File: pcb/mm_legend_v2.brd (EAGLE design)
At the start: 100 x 80 mm, 76 parts, among them IC1 ULN2003AD, IC2 TB6612FNG

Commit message: pcb: minor changes in pcb and schematic.
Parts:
- C17: value 100u -> 100n
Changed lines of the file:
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@@
 <element name="C15" library="resistor" package="B/3528-21W" value="47u" x="11.43" y="42.244" rot="R270"/>
 <element name="C16" library="resistor" package="A/3216-18R" value="10u" x="75.692" y="49.022" rot="R270"/>
-<element name="C17" library="resistor" package="C0805K" value="100u" x="30.988" y="40.64"/>
+<element name="C17" library="resistor" package="C0805K" value="100n" x="30.988" y="40.64"/>
 <element name="C18" library="resistor" package="C/6032-28R" value="100u" x="24.638" y="34.29"/>
 <element name="C19" library="resistor" package="C0805K" value="100n" x="30.988" y="45.466"/>

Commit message: pcb: redesigned pcb.
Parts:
- moved R6 39.0 mm to (19.3, 53.8), turned to 270 degrees
- moved R8 35.7 mm to (43.9, 57.7), turned to 90 degrees
- moved R7 35.0 mm to (16.5, 53.8), turned to 90 degrees
- moved R9 32.3 mm to (40.7, 57.7)
- moved R5 16.4 mm to (18.9, 46.0), turned to 270 degrees
- moved BAT_LED 15.6 mm to (18.9, 41.4), turned to 0 degrees
- moved R21 12.5 mm to (77.5, 65.5), turned to 270 degrees
- moved C18 11.8 mm to (26.2, 46.0)
- moved R20 11.5 mm to (85.6, 21.3), turned to 180 degrees
- moved L1 11.4 mm to (7.54, 35.6), turned to 0 degrees
- moved R10 9.80 mm to (76.5, 54.1)
- moved C20 9.74 mm to (28.2, 43.2), turned to 180 degrees
- moved C3 9.58 mm to (73.7, 38.4)
- moved C17 9.57 mm to (39.9, 37.1), turned to 90 degrees
- moved C19 9.45 mm to (38.6, 39.9)
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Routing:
- net GND: track 70.8 -> 237.8 mm, vias 14 -> 6
- net VBAT: track 108.6 -> 57.8 mm, vias 4 -> 2
- net MOTOR2_PWM: track 50.3 -> 83.1 mm, vias 2 -> 6
- net MOTOR1_PWM: track 50.7 -> 72.9 mm, vias 2 -> 6
- net N$15: track 2.39 -> 20.7 mm, vias 0 -> 2
- net PHOTO_FRONT_R: track 45.1 -> 63.4 mm
- net UI_LED: track 44.2 -> 26.9 mm, vias 0 -> 2
- net N$16: track 5.54 -> 22.1 mm, vias 0 -> 2
- net N$22: track 19.8 -> 6.08 mm
- net MOTOR2_CH1: track 43.8 -> 31.5 mm
- net N$8: track 43.6 -> 31.3 mm
- net N$10: track 17.9 -> 5.75 mm
- net MOTOR1_CH2: track 40.4 -> 29.3 mm
- net N$14: track 47.2 -> 36.7 mm
- net N$20: track 7.23 -> 17.4 mm
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
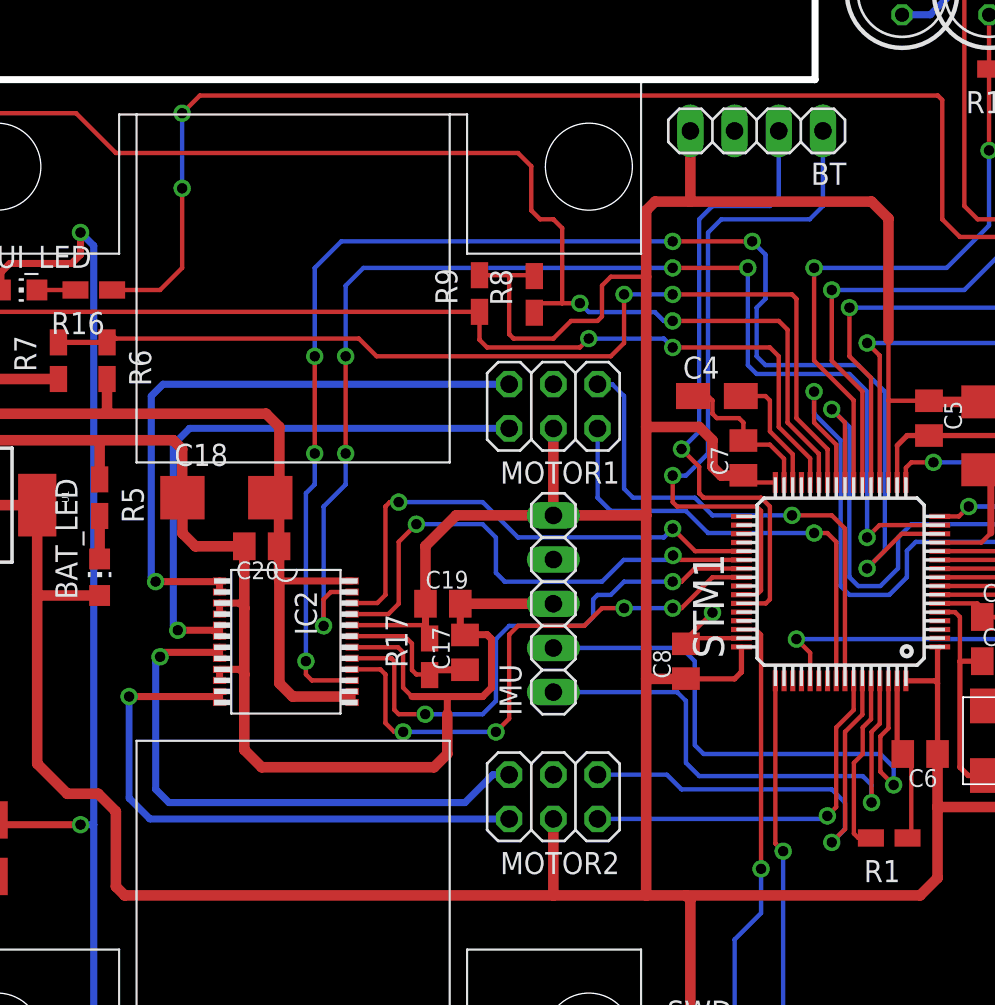
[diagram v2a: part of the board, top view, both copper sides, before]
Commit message: pcb: update pcb and schematic.
Changes:
- Moved BT connector away from motor holder.
- Changed pinout of motor connectors - fix issue #1.
- Added thicker lines for motor + and - signals.
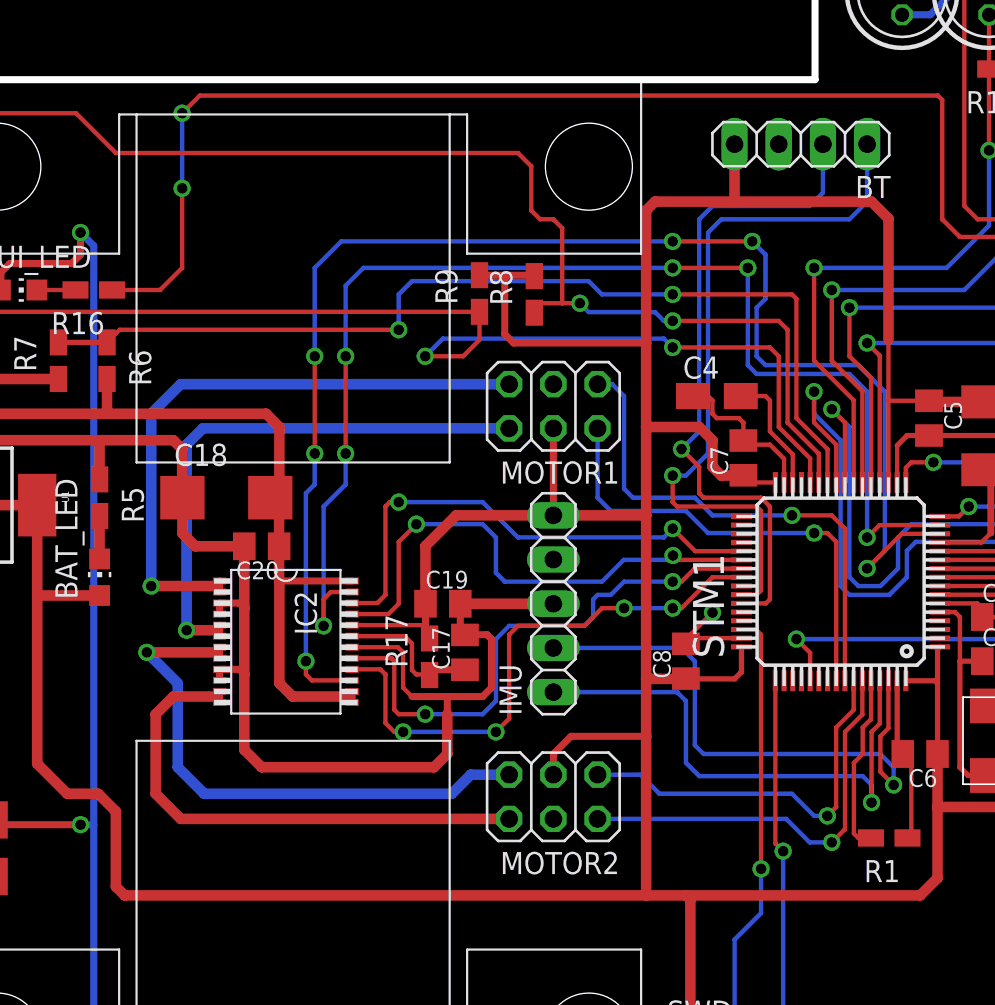
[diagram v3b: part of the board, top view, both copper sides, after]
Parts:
- moved BT 2.65 mm to (59.2, 66.3)
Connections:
- net 3V3: now also MOTOR2.3; no longer MOTOR2.4
- net ENC2_A: now also MOTOR2.1; no longer MOTOR2.2
- net ENC2_B: now also MOTOR2.2; no longer MOTOR2.1
- net GND: now also MOTOR2.4; no longer MOTOR2.3
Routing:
- net SW2: track 68.8 -> 75.5 mm
- net N$28: track 34.1 -> 30.3 mm, vias 1 -> 0
- net ENC2_B: track 27.5 -> 24.0 mm
- net USART_TX: track 39.4 -> 41.1 mm
- net USART_RX: track 36.9 -> 38.6 mm
- net N$24: track 33.6 -> 32.3 mm
- net VBAT: track 57.8 -> 56.8 mm
- net ENC2_A: track 21.7 -> 22.6 mm
- net N$30: track 33.3 -> 32.4 mm

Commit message: pcb: updated vbat resistors to real values.
Until now resistor values were 20k and 100k. 20k resistor doesn't exist in the series.
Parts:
- R3: value 100k -> 68k
- R4: value 20k -> 13k
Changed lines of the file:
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@@
 <element name="R22" library="resistor" package="R0805W" value="1k" x="91.186" y="28.956" rot="R90"/>
 <element name="R23" library="resistor" package="R0805W" value="1k" x="94.996" y="54.356" rot="R270"/>
-<element name="R3" library="resistor" package="R0805W" value="100k" x="9.144" y="27.512"/>
-<element name="R4" library="resistor" package="R0805W" value="20k" x="8.128" y="24.304" rot="R90"/>
+<element name="R3" library="resistor" package="R0805W" value="68k" x="9.144" y="27.512"/>
+<element name="R4" library="resistor" package="R0805W" value="13k" x="8.128" y="24.304" rot="R90"/>
 <element name="R5" library="resistor" package="R0805W" value="1k" x="18.876" y="45.974" rot="R270"/>
 <element name="R6" library="resistor" package="R0805W" value="100k" x="19.304" y="53.848" rot="R270"/>

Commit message: pcb: fix motor connector wiring.
Fix issue #1.
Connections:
- net 3V3: now also MOTOR1.3; no longer MOTOR1.4
- net GND: now also MOTOR1.4; no longer MOTOR1.3
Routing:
- net 3V3: track 273.9 -> 271.3 mm
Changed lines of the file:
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@@
 <wire x1="93.218" y1="57.658" x2="93.218" y2="58.166" width="0.3048" layer="16"/>
 <contactref element="MOTOR2" pad="4"/>
-<contactref element="MOTOR1" pad="3"/>
+<contactref element="MOTOR1" pad="4"/>
 </signal>
 <signal name="N$3">
@@
 <wire x1="45.974" y1="32.258" x2="50.292" y2="32.258" width="0.4064" layer="1"/>
 <wire x1="43.8112" y1="58.7613" x2="43.862" y2="58.7105" width="0.4064" layer="1"/>
-<contactref element="MOTOR1" pad="4"/>
 <contactref element="MOTOR2" pad="3"/>
 <wire x1="44.958" y1="31.242" x2="44.958" y2="30.052" width="0.4064" layer="1"/>
-<wire x1="44.958" y1="49.958" x2="44.958" y2="44.958" width="0.4064" layer="1"/>
 <wire x1="40.7124" y1="58.7613" x2="42.164" y2="58.7613" width="0.4064" layer="1"/>
 <wire x1="43.862" y1="58.7613" x2="43.862" y2="58.7105" width="0.4064" layer="1"/>
@@
 <wire x1="42.164" y1="58.7613" x2="42.164" y2="55.372" width="0.4064" layer="1"/>
 <wire x1="42.164" y1="55.372" x2="42.672" y2="54.864" width="0.4064" layer="1"/>
-<wire x1="42.672" y1="54.864" x2="50.292" y2="54.864" width="0.4064" layer="1"/>
+<wire x1="42.672" y1="54.864" x2="44.958" y2="54.864" width="0.4064" layer="1"/>
+<contactref element="MOTOR1" pad="3"/>
+<wire x1="44.958" y1="54.864" x2="50.292" y2="54.864" width="0.4064" layer="1"/>
+<wire x1="44.958" y1="52.498" x2="44.958" y2="54.864" width="0.4064" layer="1"/>
 </signal>
 <signal name="AVDD">

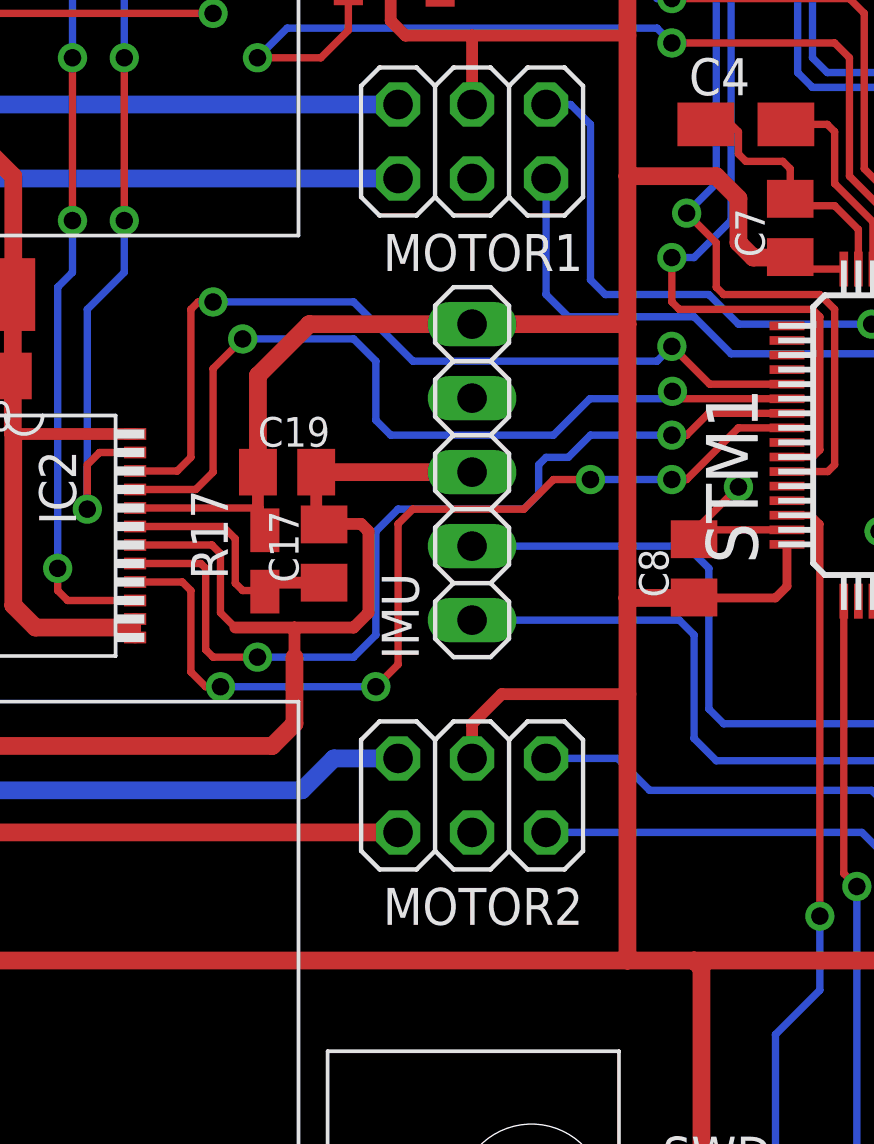
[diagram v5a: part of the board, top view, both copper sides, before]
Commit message: pcb: reroute paths to h-bridge around imu sensor.
Fixes issue #6.
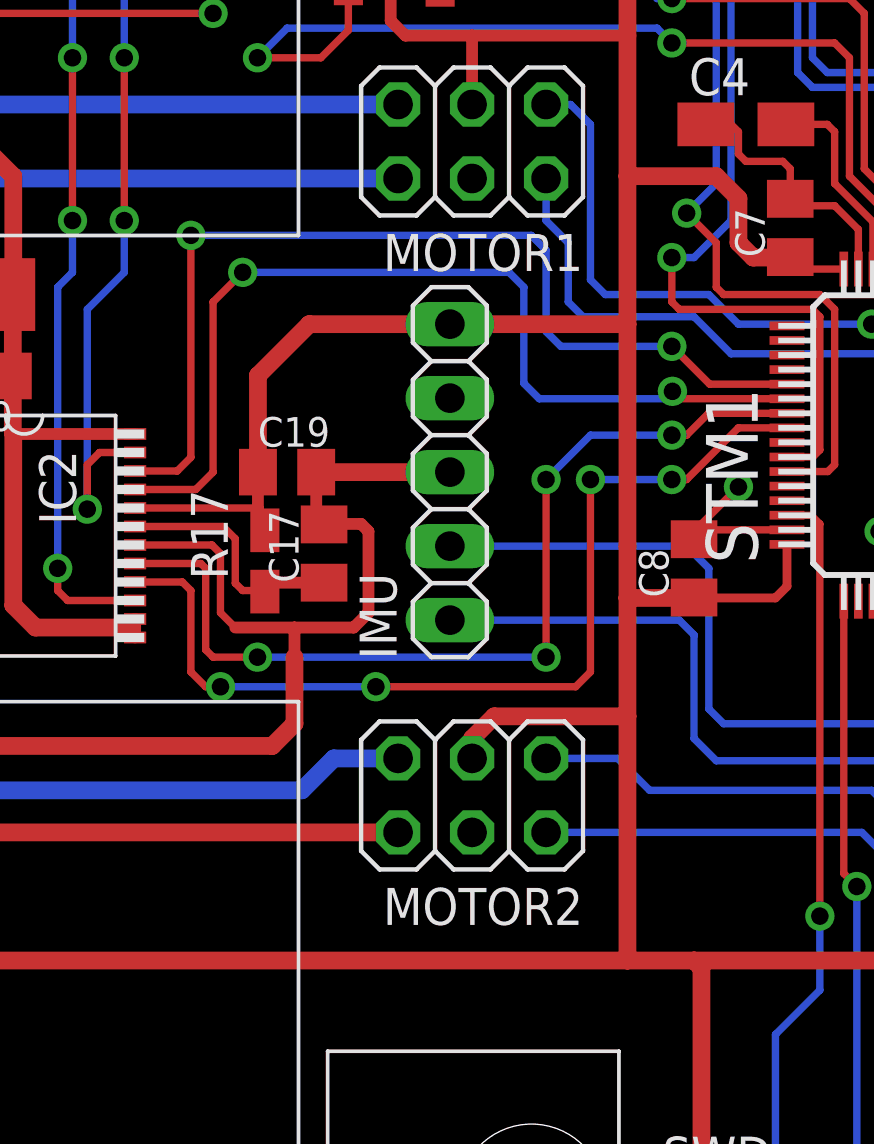
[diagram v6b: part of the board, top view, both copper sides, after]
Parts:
- moved IMU 0.76 mm to (44.2, 39.9)
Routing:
- net MOTOR1_CH2: track 29.3 -> 33.9 mm
- net MOTOR1_CH1: track 29.9 -> 32.8 mm
- net MOTOR2_CH2: track 32.0 -> 33.1 mm
- net MOTOR2_CH1: track 31.5 -> 32.4 mm, vias 2 -> 4
- net I2C_SDA: track 32.7 -> 33.5 mm
- net I2C_SCL: track 30.8 -> 31.6 mm
- net GND: track 237.8 -> 237.0 mm
- net 3V3: track 271.3 -> 270.7 mm

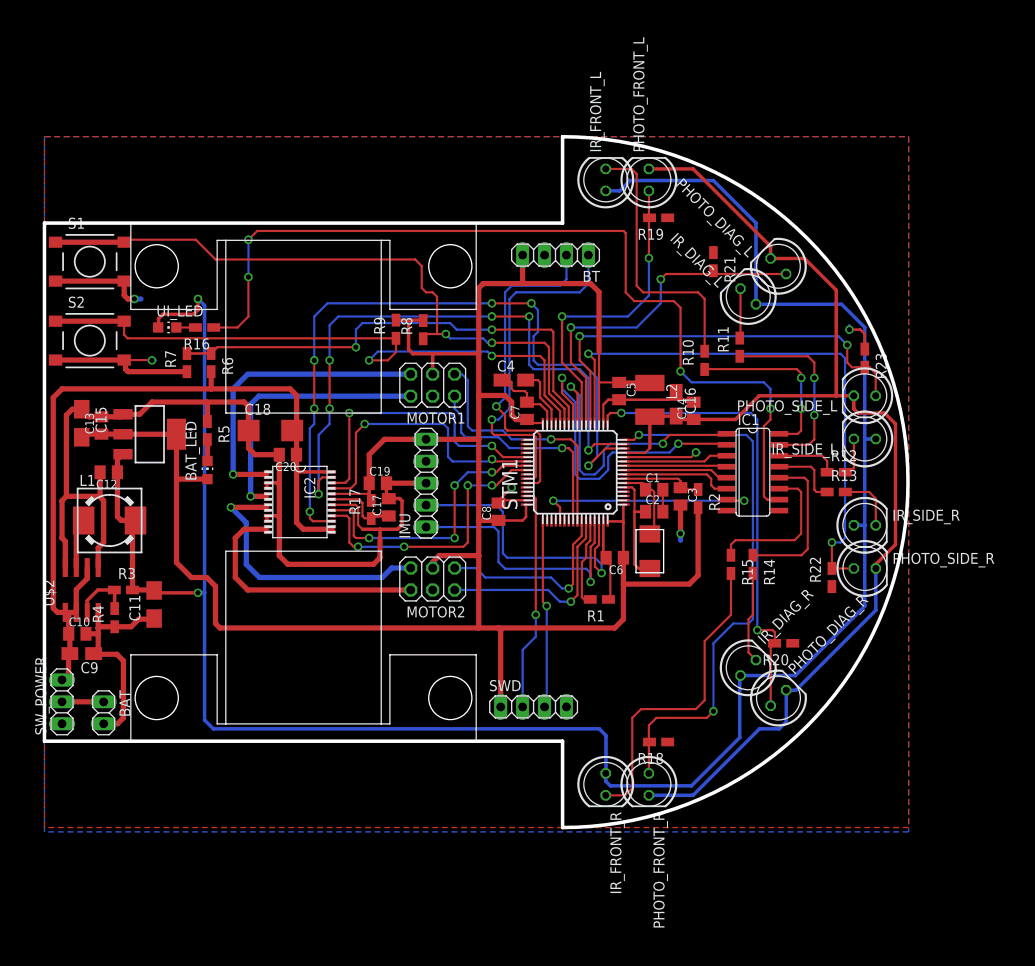
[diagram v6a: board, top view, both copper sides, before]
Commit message: pcb: move status led to the front.
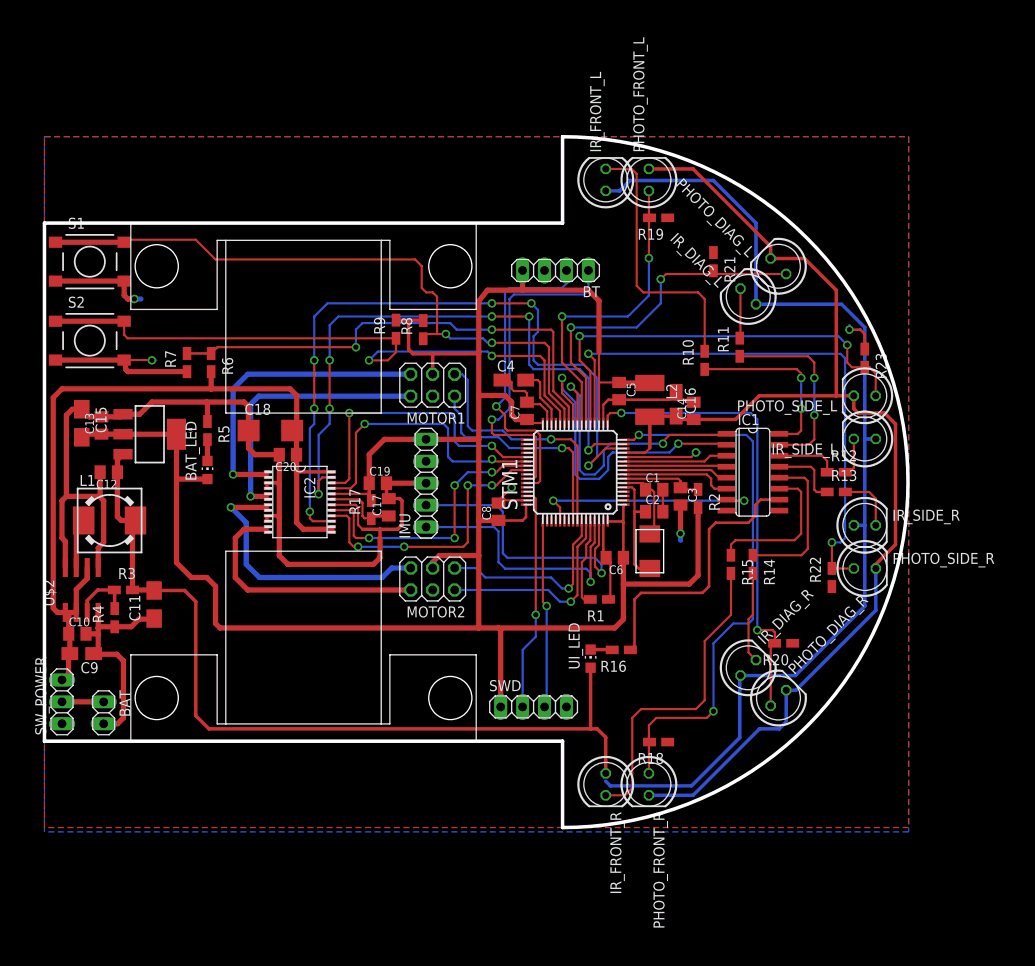
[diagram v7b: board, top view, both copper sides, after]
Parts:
- moved UI_LED 62.2 mm to (63.2, 19.6), turned to 0 degrees
- moved R16 61.0 mm to (66.8, 20.6)
- moved BT 1.78 mm to (59.2, 64.5)
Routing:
- net N$21: track 104.9 -> 32.2 mm, vias 4 -> 0
- net +5V: track 256.2 -> 219.7 mm, vias 2 -> 0
- net 3V3: track 270.7 -> 267.7 mm
- net USART_RX: track 38.6 -> 37.1 mm
- net USART_TX: track 41.1 -> 39.7 mm

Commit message: pcb: change wall sensor placement.
Fixes #7.
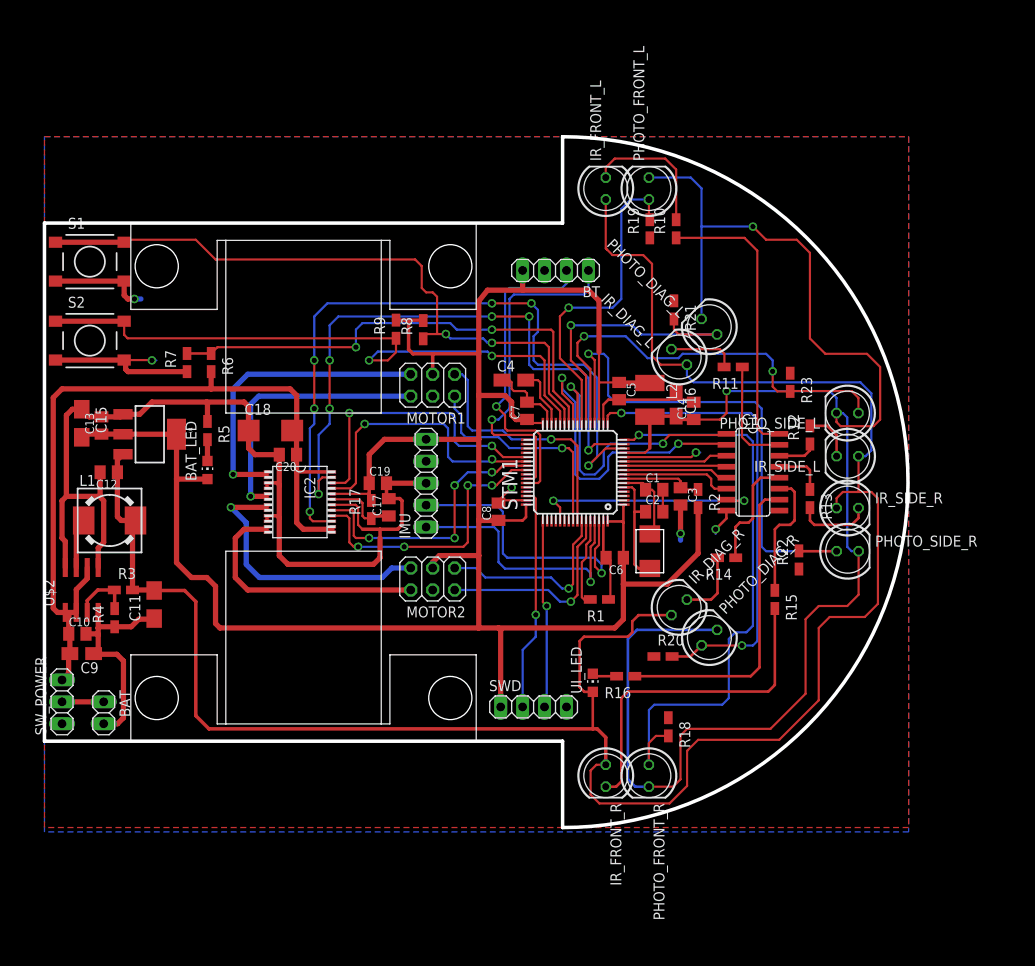
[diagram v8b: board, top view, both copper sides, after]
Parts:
- moved R10 15.6 mm to (73.2, 69.3)
- moved R20 14.1 mm to (71.6, 19.8), turned to 0 degrees
- moved IR_DIAG_L 10.6 mm to (73.5, 54.5)
- moved IR_DIAG_R 10.6 mm to (73.5, 25.5)
- moved PHOTO_DIAG_L 10.6 mm to (77.0, 58.0)
- moved PHOTO_DIAG_R 10.6 mm to (77.0, 22.0)
- moved R23 9.08 mm to (86.4, 51.6)
- moved R21 7.22 mm to (72.9, 59.9)
- moved R15 6.51 mm to (84.6, 26.4)
- moved R12 5.29 mm to (88.6, 45.5), turned to 90 degrees
- moved R22 4.32 mm to (87.4, 31.0)
- moved R13 3.14 mm to (88.6, 38.1), turned to 270 degrees
- moved R14 3.14 mm to (79.0, 31.2), turned to 180 degrees
- moved R16 3.09 mm to (67.3, 17.5)
- moved IR_SIDE_L 2.83 mm to (93.0, 43.0)
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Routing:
- net AVDD: track 139.2 -> 196.0 mm, vias 0 -> 2
- net +5V: track 219.7 -> 251.7 mm
- net N$8: track 31.3 -> 16.1 mm
- net N$15: track 20.7 -> 33.4 mm, vias 2 -> 0
- net N$16: track 22.1 -> 12.8 mm, vias 2 -> 0
- net PHOTO_DIAG_L: track 41.2 -> 35.9 mm, vias 2 -> 1
- net PHOTO_FRONT_R: track 63.4 -> 68.3 mm, vias 2 -> 1
- net N$19: track 18.0 -> 13.3 mm
- net N$21: track 32.2 -> 36.2 mm
- net PHOTO_SIDE_R: track 66.4 -> 62.8 mm, vias 2 -> 1
- net N$13: track 10.6 -> 7.95 mm
- net N$17: track 7.08 -> 4.52 mm
- net N$20: track 17.4 -> 15.0 mm
- net N$14: track 36.7 -> 39.0 mm
- net N$10: track 5.75 -> 7.90 mm
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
